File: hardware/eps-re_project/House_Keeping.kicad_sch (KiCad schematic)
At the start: 4 parts, among them Q1 SI2302

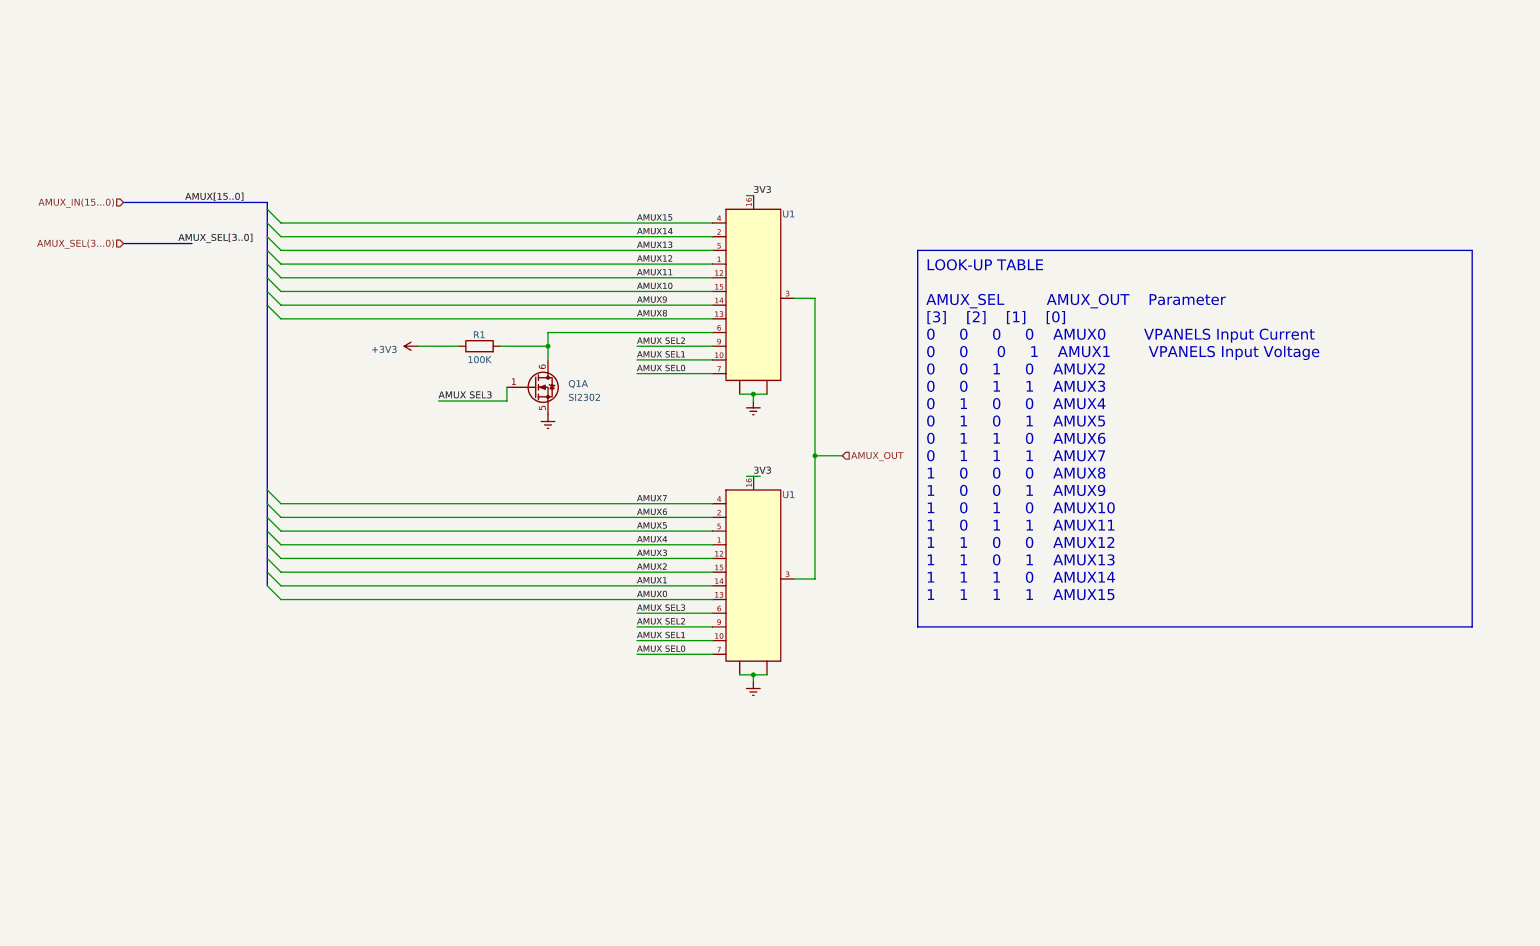
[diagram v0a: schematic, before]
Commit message: hardware: Restructuring the circuit, modifying symbols, footprints and other corrections
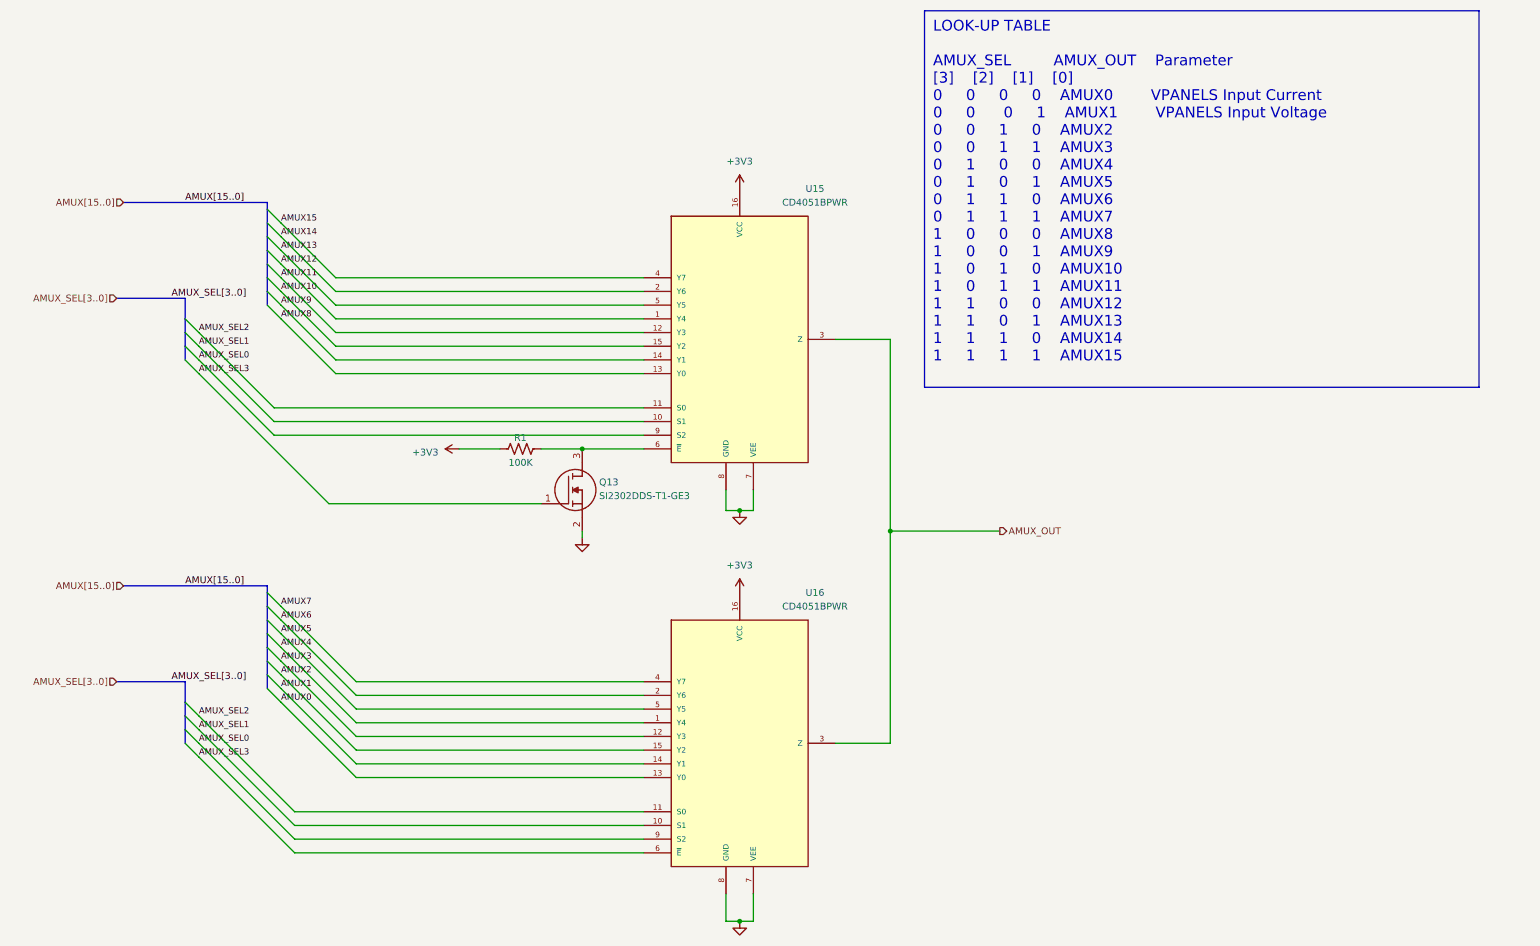
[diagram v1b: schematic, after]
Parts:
- removed Q1: SI2302, symbol Device:Q_Dual_NMOS_G1S2G2D2S1D1
- removed U1 (x2): ~, symbol New_Library:U_multiplex
- added Q13: SI2302DDS-T1-GE3, footprints:SI2302DDS-T1-GE3, symbol SI2302DDS-T1-GE3:SI2302DDS-T1-GE3
- added U15, U16: CD4051BPWR, footprints:CD4051BPWR, symbol CD4051BPWR:CD4051BPWR
- R1: symbol Device:R -> Device:R_US
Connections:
- net +3V3: now also U15.16 (VCC), U16.16 (VCC)
- net AMUX0: now also U16.13 (Y0)
- net AMUX1: now also U16.14 (Y1)
- net AMUX10: now also U15.15 (Y2)
- net AMUX11: now also U15.12 (Y3)
- net AMUX12: now also U15.1 (Y4)
- net AMUX13: now also U15.5 (Y5)
- net AMUX14: now also U15.2 (Y6)
- net AMUX15: now also U15.4 (Y7)
- net AMUX2: now also U16.15 (Y2)
- net AMUX3: now also U16.12 (Y3)
- net AMUX4: now also U16.1 (Y4)
- net AMUX5: now also U16.5 (Y5)
- net AMUX6: now also U16.2 (Y6)
- net AMUX7: now also U16.4 (Y7)
- net AMUX8: now also U15.13 (Y0)
- net AMUX9: now also U15.14 (Y1)
- net AMUX_OUT: now also U15.3 (Z), U16.3 (Z)
- net at R1.2: now also Q13.3 (D), U15.6 (~{E})
- new net AMUX_SEL0: U15.9 (S2), U16.9 (S2)
- new net AMUX_SEL1: U15.10 (S1), U16.10 (S1)
- new net AMUX_SEL2: U15.11 (S0), U16.11 (S0)
- new net AMUX_SEL3: Q13.1 (G), U16.6 (~{E})
- new net GND: Q13.2 (S), U15.7 (VEE), U15.8 (GND), U16.7 (VEE), U16.8 (GND)
